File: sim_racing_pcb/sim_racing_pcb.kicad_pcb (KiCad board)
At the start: 2 copper layers, 100 x 50 mm, 25 parts, among them J1 Pedales MicroUsb, J10 Encoder - IZQ, J11 Display TFT, J12 GND, J13 GND, J14 3V3, J15 5V, J2 Paddle_Shift_R, J3 Paddle_Shift_L, J4 BTN 1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

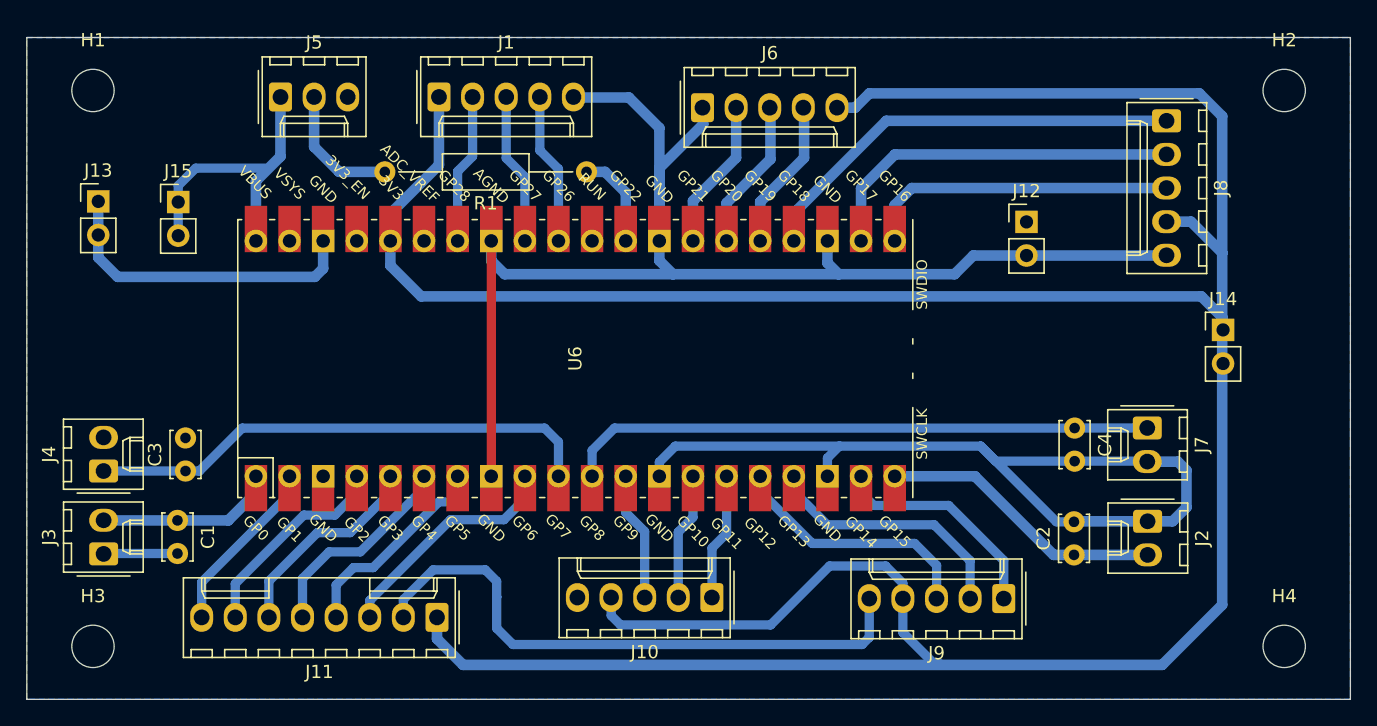
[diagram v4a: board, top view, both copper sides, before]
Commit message: modify position of buttons
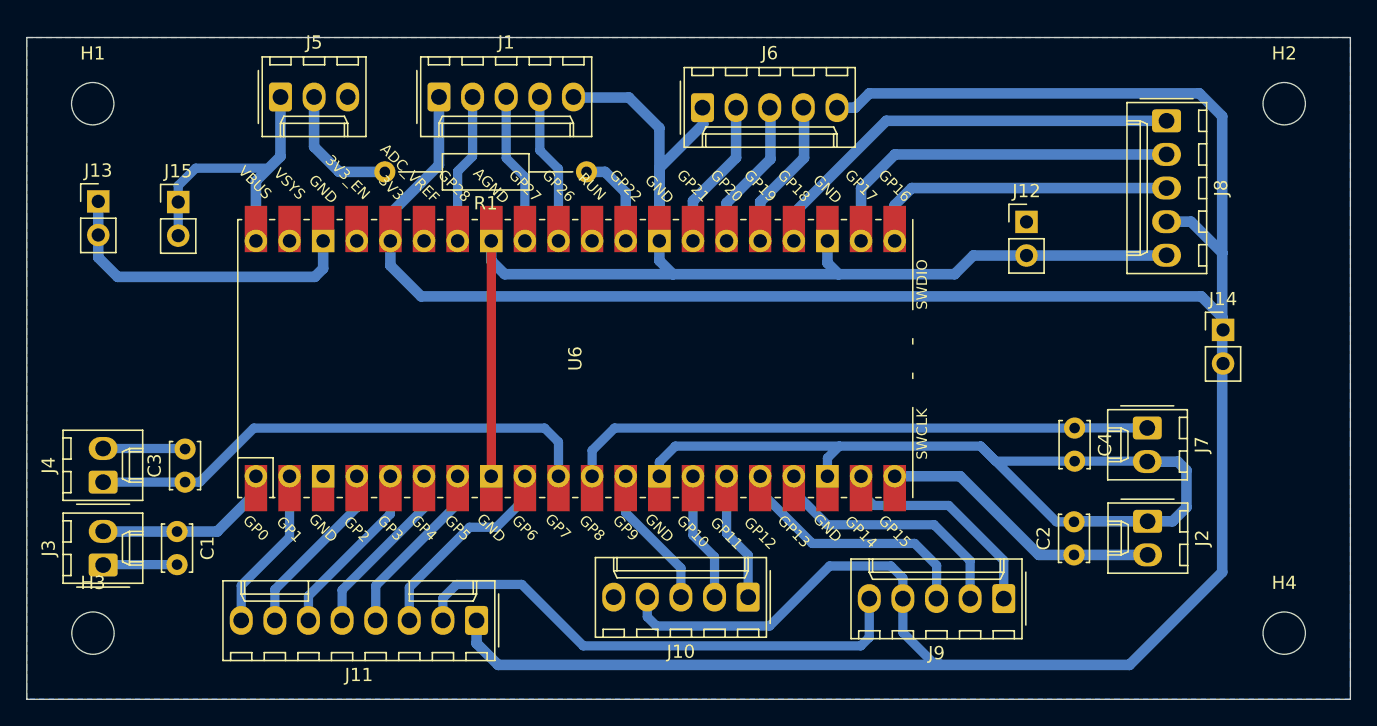
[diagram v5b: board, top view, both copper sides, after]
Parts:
- moved J11 3.00 mm to (134.0, 64.0)
- moved J10 2.74 mm to (154.5, 62.3)
- moved H1 1.00 mm to (105.0, 25.0)
- moved H2 1.00 mm to (195.0, 25.0)
- moved H3 1.00 mm to (105.0, 65.0)
- moved H4 1.00 mm to (195.0, 65.0)
- moved J4 0.84 mm to (105.8, 53.6)
- moved C3 0.84 mm to (112.0, 53.6)
- moved C1 0.84 mm to (111.3, 57.3)
- moved J3 0.84 mm to (105.8, 59.9)
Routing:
- net +3V3: track 249.4 -> 242.6 mm
- net DIS - MOSI: track 15.9 -> 13.5 mm
- net DIS - DC: track 15.8 -> 13.5 mm
- net DIS - CLK: track 15.8 -> 13.5 mm
- net DIS - RST: track 15.8 -> 13.5 mm
- net DIS - CS: track 17.9 -> 15.7 mm
- net SW - IZQ: track 10.1 -> 11.2 mm
- net DIS - LED: track 13.4 -> 12.4 mm
- net GND: track 245.4 -> 246.0 mm

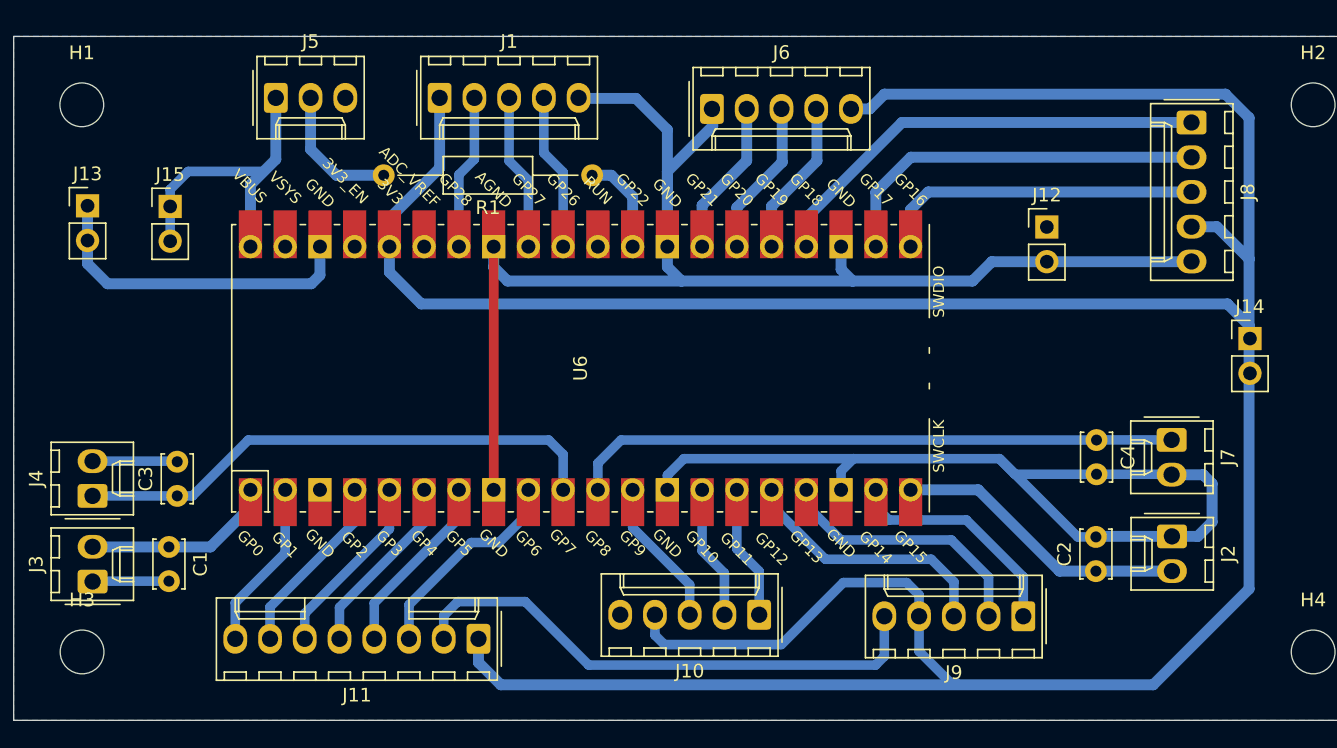
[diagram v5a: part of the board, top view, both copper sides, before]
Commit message: Modify usb and as5600 connectors for unique 6 cable molex
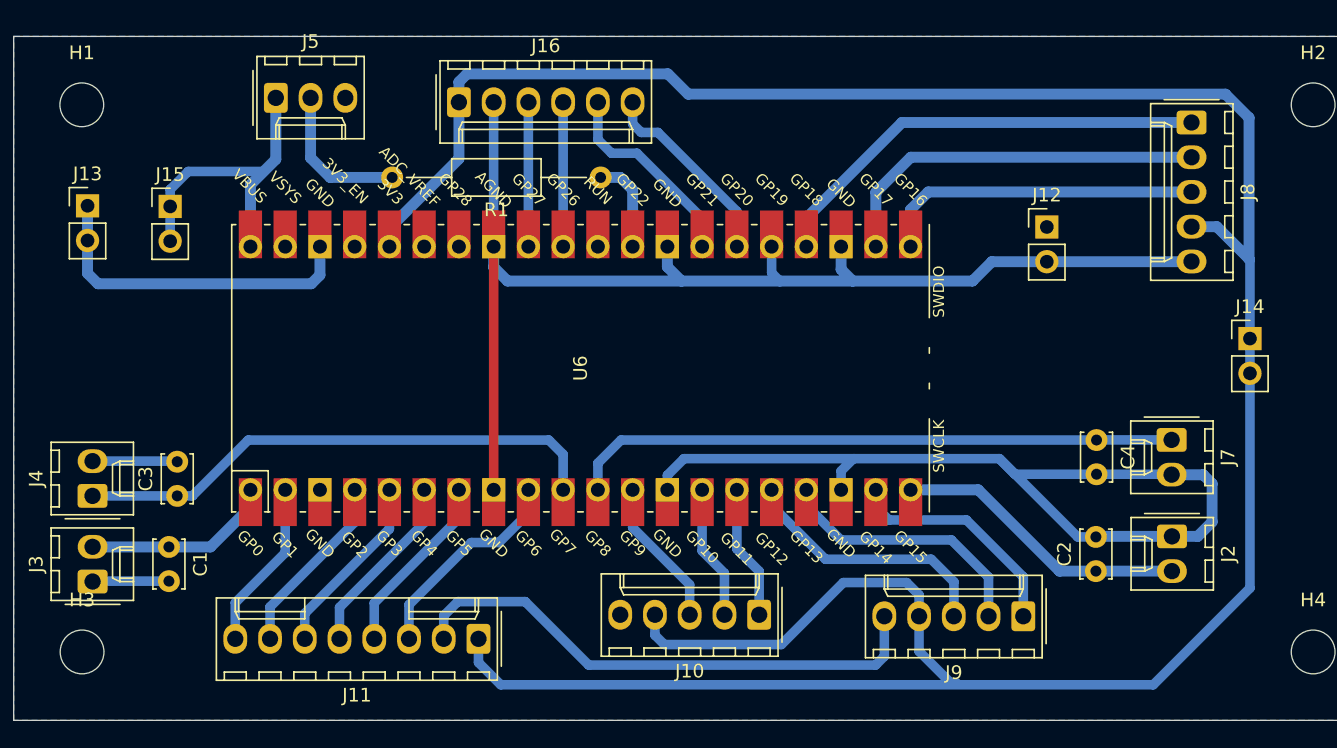
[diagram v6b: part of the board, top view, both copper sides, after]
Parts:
- removed J1: Pedales MicroUsb, Connector_Molex:Molex_KK-254_AE-6410-05A_1x05_P2.54mm_Vertical
- removed J6: AS5600, Connector_Molex:Molex_KK-254_AE-6410-05A_1x05_P2.54mm_Vertical
- added J16: EXTERN, Connector_Molex:Molex_KK-254_AE-6410-06A_1x06_P2.54mm_Vertical, F.Cu at (132.6, 24.8)
- moved R1 0.64 mm to (142.9, 30.3)
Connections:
- U6 pad 25: DIR -> GND
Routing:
- net +3V3: track 242.6 -> 206.0 mm
- net GND: track 246.0 -> 232.3 mm
- net DIR: track 11.5 -> 0.00 mm
- net A2-Clutch: track 11.3 -> 0.00 mm
- net SCL: track 11.4 -> 14.8 mm
- net SDA: track 11.5 -> 14.4 mm
- net Net-(J5-Pin_2): track 9.89 -> 10.9 mm
- net A1-Brk: track 11.5 -> 10.6 mm
- net A0-Acc: track 11.5 -> 10.6 mm
